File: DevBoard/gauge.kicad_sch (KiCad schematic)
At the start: 78 parts, among them J101 Pack (welded 4S) - use instea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, J102 Cell 1 NTC 10k 103AT, J103 EV2400 SMBus, J104 Bench PACK_P, J105 Cell 2 NTC 10k 103AT, J106 Cell 3 NTC 10k 103AT, J107 Cell 4 NTC 10k 103AT, Q101 AGM404AP1, Q102 AGM404AP1, Q103 AO3400A, Q104 AO3400A, SW101 WAKE, U101 BQ40Z50RSMR-R2, U102 BQ294700DSGR

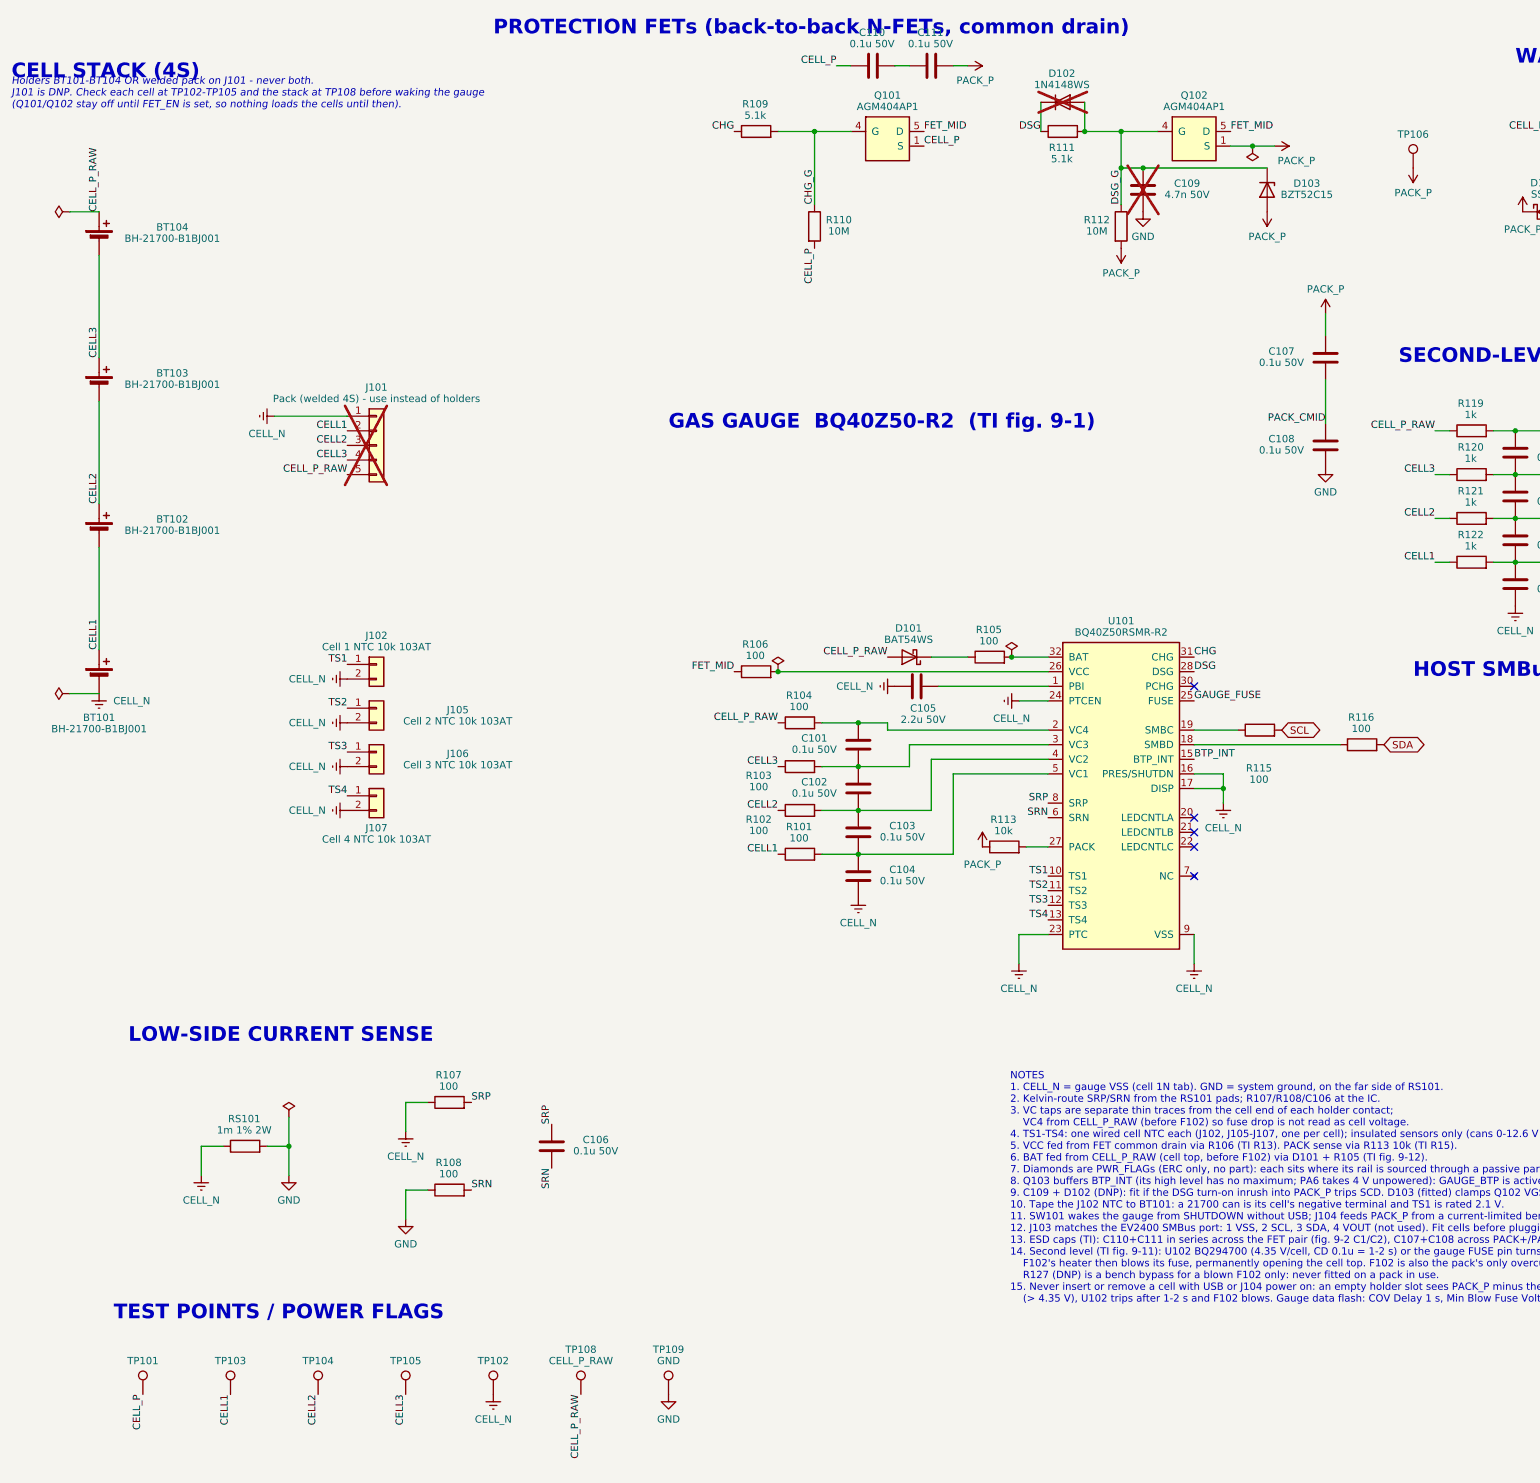
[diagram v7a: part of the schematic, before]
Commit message: Dev board schematic: tidy pass
- Title blocks on every sheet: rev A6, 2026-10-14, status line updated
  (was "Not reviewed, laid out, built or tested"); tidy_fields.py
  writes the same.
- Port sheet: the TPD4S201 block is titled with liquid detection
  ("CC/SBU PROTECTION (TPD4S201) + LIQUID DETECTION") and moved clear of
  the heading it collided with; I2Cc heading moved next to the EEPROM;
  PP5V heading clear of U405's GND.
- MCU sheet: test-point row out of the title block, with a heading;
  long NOTES lines wrapped inside the page border.
- Gauge sheet: cell-stack heading clear of its note; TP106 joins the
  test-point row.
- Top sheet: sheet index updated (BQ294700, TPD4S201, TH1-TH5) and
  spaced from the strap note and revision log; rev log line for the
  placement and this tidy.
- New tools/move_region.py moves a rectangle of a sheet (symbols,
  fields, wires, labels) by an offset.

Netlist identical before and after (265 nets); ERC 0 errors;
check_overlaps TOTAL 0.

Co-Authored-By: Claude Opus 5.5 <noreply@anthropic.com>
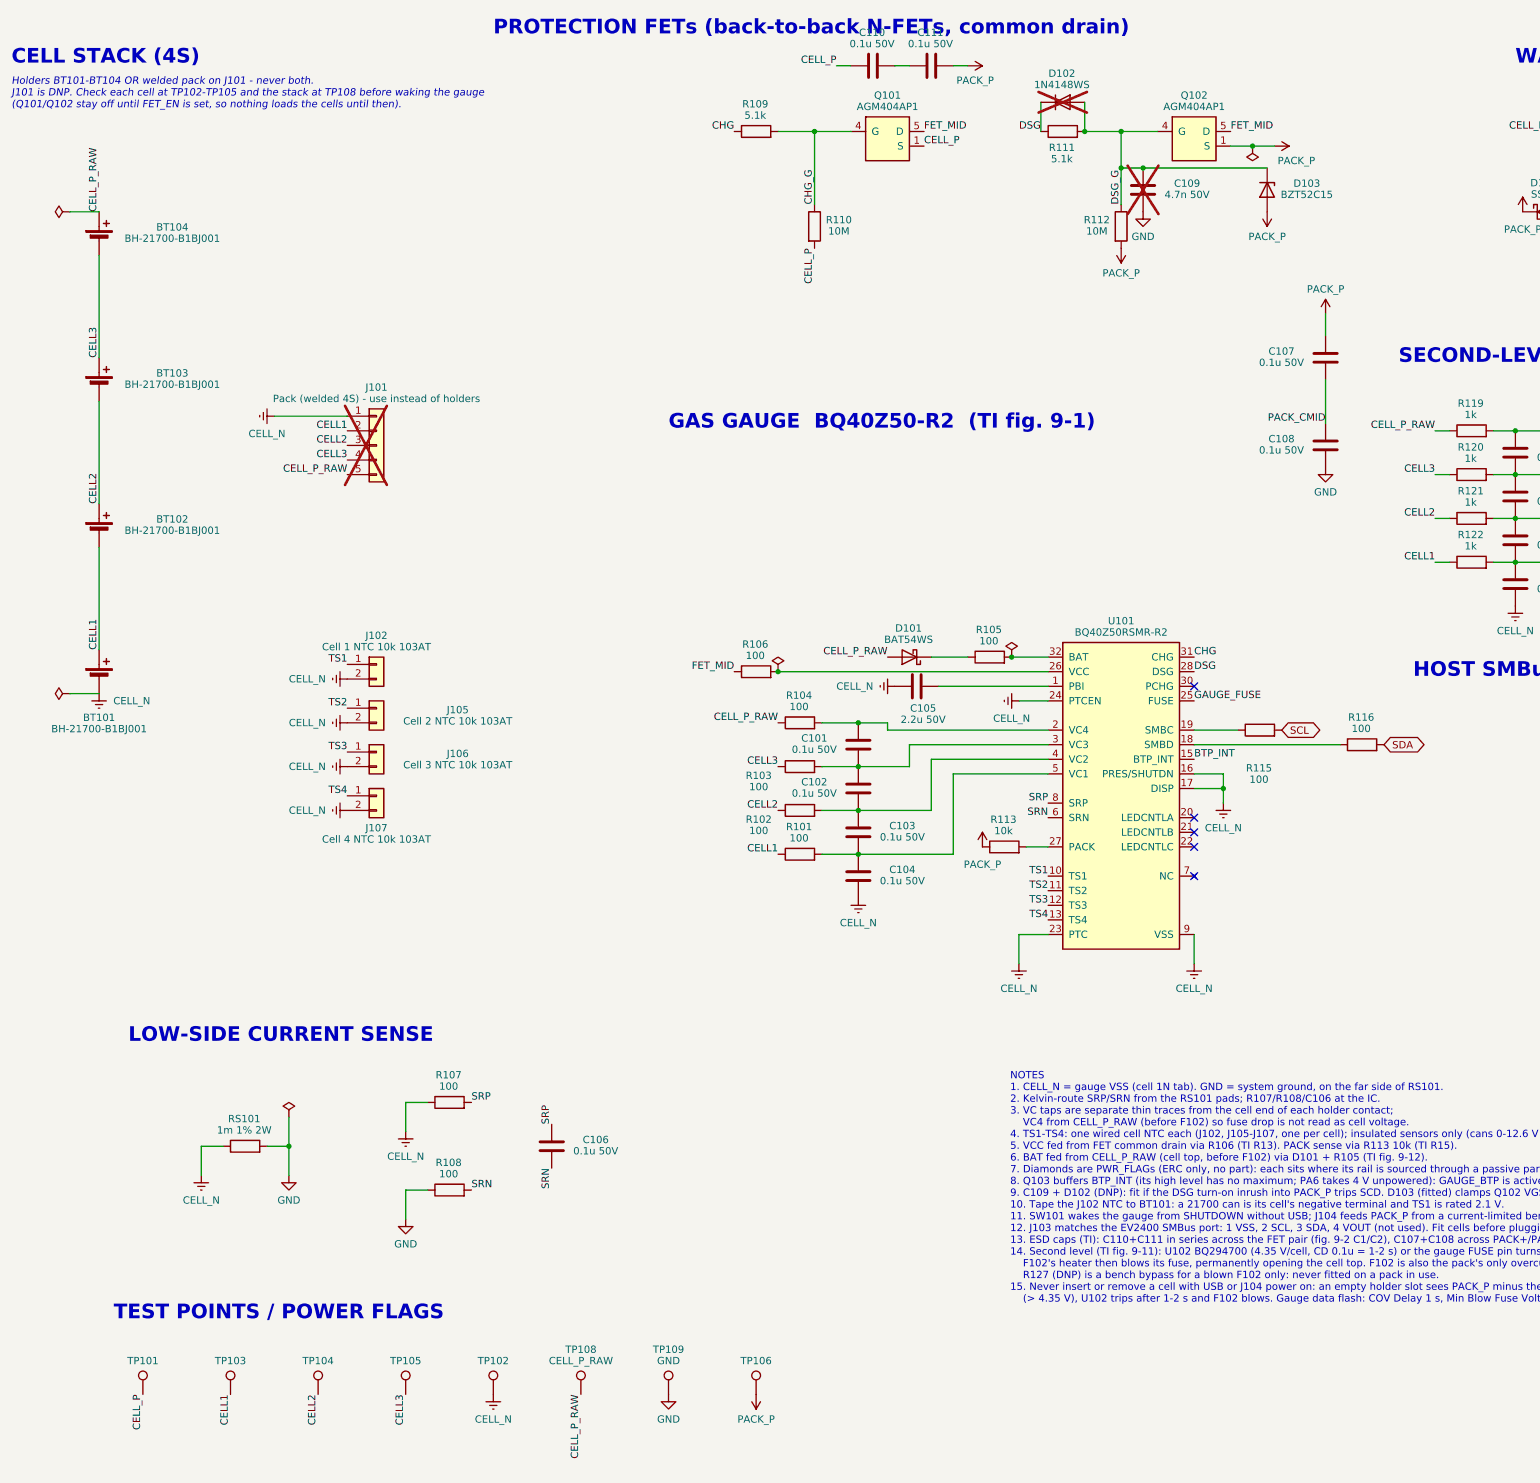
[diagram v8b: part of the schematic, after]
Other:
- moved on the sheet: TP106
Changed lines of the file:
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@@
 	(title_block
 		(title "Cells and gauge")
-		(date "2026-10-11")
-		(rev "A (draft)")
+		(date "2026-10-14")
+		(rev "A6")
 		(company "Monolith 100 W battery bank - dev board")
 		(comment 1 "4S input, BQ40Z50-R2 gauge/protector, protection FETs")
 		(comment 2 "Spec + open items: DevBoard/README.md")
-		(comment 3 "Not reviewed, laid out, built or tested")
+		(comment 3 "Reviewed 3x (docs/devboard); board placed, not routed or built")
 	)
 	(text "LOW-SIDE CURRENT SENSE"
@@
 	(text "CELL STACK (4S)"
 		(exclude_from_sim no)
-		(at 22.86 35.56 0)
+		(at 22.86 33.02 0)
 		(effects
 			(font
@@
 	(symbol
 		(lib_id "Connector:TestPoint")
-		(at 266.7 50.8 0)
+		(at 152.4 264.16 0)
 		(unit 1)
 		(body_style 1)
@@
 		(dnp no)
 		(property "Reference" "TP106"
-			(at 266.70 44.95 0)
+			(at 152.4 258.31 0)
 			(show_name no)
 			(do_not_autoplace no)
@@
 		)
 		(property "Value" "PACK_P"
-			(at 271.88 48.48 0)
+			(at 157.58 261.84 0)
 			(hide yes)
 			(show_name no)
@@
 		)
 		(property "Footprint" "TestPoint:TestPoint_Pad_D1.5mm"
-			(at 271.78 50.8 0)
+			(at 157.48 264.16 0)
 			(hide yes)
 			(show_name no)
@@
 		)
 		(property "Datasheet" ""
-			(at 271.78 50.8 0)
+			(at 157.48 264.16 0)
 			(hide yes)
 			(show_name no)
@@
 		)
 		(property "Description" "test point"
-			(at 266.7 50.8 0)
+			(at 152.4 264.16 0)
 			(hide yes)
 			(show_name no)
@@
 	(symbol
 		(lib_id "power:VCC")
-		(at 266.7 50.8 180)
+		(at 152.4 264.16 180)
 		(unit 1)
 		(body_style 1)
@@
 		(dnp no)
 		(property "Reference" "#PWR122"
-			(at 266.7 50.8 0)
+			(at 152.4 264.16 0)
 			(hide yes)
 			(show_name no)
@@
 		)
 		(property "Value" "PACK_P"
-			(at 266.70 55.12 0)
+			(at 152.4 268.48 0)
 			(show_name no)
 			(do_not_autoplace no)
@@
 		)
 		(property "Footprint" ""
-			(at 266.7 50.8 0)
+			(at 152.4 264.16 0)
 			(hide yes)
 			(show_name no)
@@
 		)
 		(property "Datasheet" ""
-			(at 266.7 50.8 0)
+			(at 152.4 264.16 0)
 			(hide yes)
 			(show_name no)
@@
 		)
 		(property "Description" "Power symbol creates a global label with name \"VCC\""
-			(at 266.7 50.8 0)
+			(at 152.4 264.16 0)
 			(hide yes)
 			(show_name no)
